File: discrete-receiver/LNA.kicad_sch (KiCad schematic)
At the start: 6 parts, among them U16 PSA4-5043_

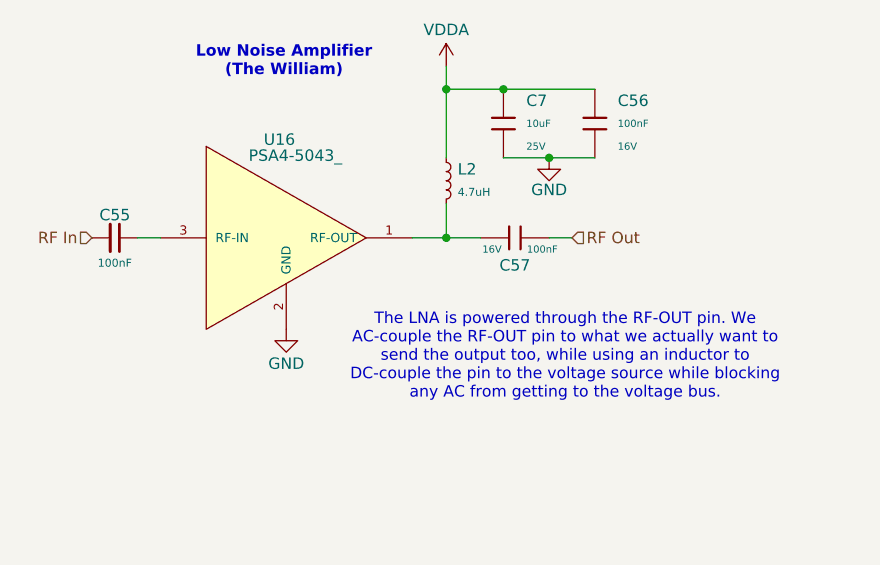
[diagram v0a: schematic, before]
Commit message: Parts on receiver page have been JLC'd and given footprints
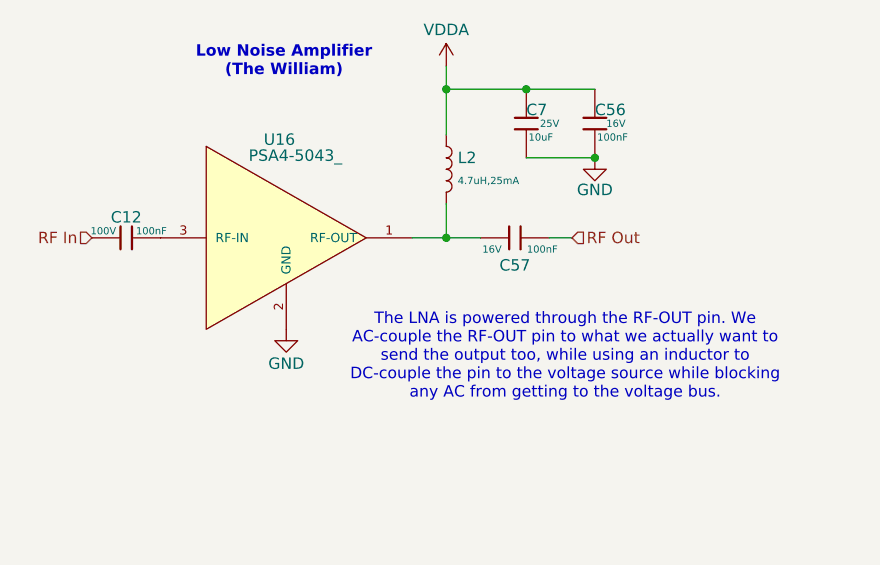
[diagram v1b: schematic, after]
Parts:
- removed C55: 100nF, symbol Device:C_Small
- removed L2: 4.7uH, symbol Device:L_Small
- added C12: 100nF, PCM_JLCPCB:C_0805, symbol PCM_JLCPCB-Capacitors:0805,100nF
- added L2: 4.7uH,25mA, PCM_JLCPCB:L_1206, symbol PCM_JLCPCB-Inductors:4.7uH,25mA
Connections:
- net RF In: now also C12.1
- net VDDA: now also L2.1
- net at C57.1, U16.1 (RF-OUT): now also L2.2
- net at U16.3 (RF-IN): now also C12.2
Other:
- moved on the sheet: C7

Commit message: Started to redo power
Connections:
- net VDDA renamed +5V_A
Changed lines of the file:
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@@
 			)
 		)
-		(property "Value" "VDDA"
+		(property "Value" "+5V_A"
 			(at 147.32 78.486 0)
 			(show_name no)

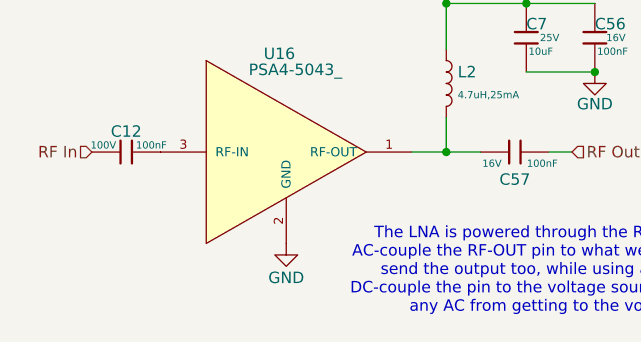
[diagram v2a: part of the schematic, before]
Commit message: Redone draft of power page
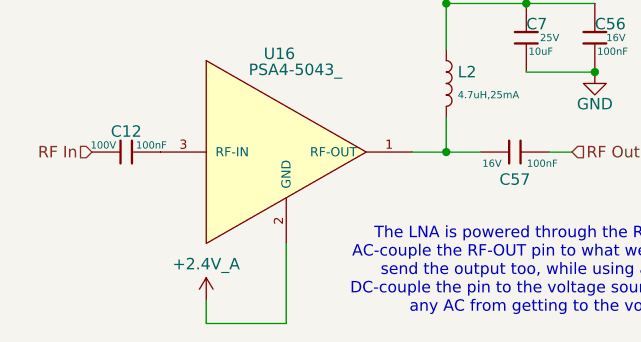
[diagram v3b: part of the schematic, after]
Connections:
- net GND: no longer U16.2 (GND), U16.4 (GND__1)
- new net +2.4V_A: U16.2 (GND), U16.4 (GND__1)
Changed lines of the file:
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@@
+	(wire
+		(pts
+			(xy 129.54 120.65) (xy 129.54 111.76)
+		)
+		(stroke
+			(width 0)
+			(type default)
+		)
+	)
 	(wire
 		(pts
@@
 		(pts
 			(xy 156.21 92.71) (xy 163.83 92.71)
+		)
+		(stroke
+			(width 0)
+			(type default)
+		)
+	)
+	(wire
+		(pts
+			(xy 120.65 120.65) (xy 129.54 120.65)
+		)
+		(stroke
+			(width 0)
+			(type default)
+		)
+	)
+	(wire
+		(pts
+			(xy 120.65 118.11) (xy 120.65 120.65)
 		)
 		(stroke
@@
 			)
 			(justify left)
+		)
+	)
+	(symbol
+		(lib_id "power:+5V")
+		(at 120.65 118.11 0)
+		(unit 1)
+		(body_style 1)
+		(exclude_from_sim no)
+		(in_bom yes)
+		(on_board yes)
+		(in_pos_files yes)
+		(dnp no)
+		(property "Reference" "#PWR0129"
+			(at 120.65 121.92 0)
+			(hide yes)
+			(show_name no)
+			(do_not_autoplace no)
+			(effects
+				(font
+					(size 1.27 1.27)
+				)
+			)
+		)
+		(property "Value" "+2.4V_A"
+			(at 120.65 114.046 0)
+			(show_name no)
+			(do_not_autoplace no)
+			(effects
+				(font
+					(size 1.27 1.27)
+				)
+			)
+		)
+		(property "Footprint" ""
+			(at 120.65 118.11 0)
+			(hide yes)
+			(show_name no)
+			(do_not_autoplace no)
+			(effects
+				(font
+					(size 1.27 1.27)
+				)
+			)
+		)
+		(property "Datasheet" ""
+			(at 120.65 118.11 0)
+			(hide yes)
+			(show_name no)
+			(do_not_autoplace no)
+			(effects
+				(font
+					(size 1.27 1.27)
+				)
+			)
+		)
+		(property "Description" "Power symbol creates a global label with name \"+5V\""
+			(at 120.65 118.11 0)
+			(hide yes)
+			(show_name no)
+			(do_not_autoplace no)
+			(effects
+				(font
+					(size 1.27 1.27)
+				)
+			)
+		)
+		(pin "1"
+		)
+		(instances
+			(project "diode_tayloe_sdr"
+				(path "/d18d178d-3f10-4d68-9036-eae71a7d091a/c96fbd90-62d0-401a-a1f5-d4c4d983c9a4/0811a985-c39e-470e-b379-1c06ccf39cf9"
+					(reference "#PWR0129")
+					(unit 1)
+				)
+			)
 		)
 	)
@@
 					(unit 1)
 				)
-			)
-		)
-	)
-	(symbol
-		(lib_id "power:GND")
-		(at 129.54 111.76 0)
-		(unit 1)
-		(body_style 1)
-		(exclude_from_sim no)
-		(in_bom yes)
-		(on_board yes)
-		(in_pos_files yes)
-		(dnp no)
-		(property "Reference" "#PWR047"
-			(at 129.54 118.11 0)
-			(hide yes)
-			(show_name no)
-			(do_not_autoplace no)
-			(effects
-				(font
-					(size 1.27 1.27)
-				)
-			)
-		)
-		(property "Value" "GND"
-			(at 129.54 115.57 0)
-			(show_name no)
-			(do_not_autoplace no)
-			(effects
-				(font
-					(size 1.27 1.27)
-				)
-			)
-		)
-		(property "Footprint" ""
-			(at 129.54 111.76 0)
-			(hide yes)
-			(show_name no)
-			(do_not_autoplace no)
-			(effects
-				(font
-					(size 1.27 1.27)
-				)
-			)
-		)
-		(property "Datasheet" ""
-			(at 129.54 111.76 0)
-			(hide yes)
-			(show_name no)
-			(do_not_autoplace no)
-			(effects
-				(font
-					(size 1.27 1.27)
-				)
-			)
-		)
-		(property "Description" "Power symbol creates a global label with name \"GND\" , ground"
-			(at 129.54 111.76 0)
-			(hide yes)
-			(show_name no)
-			(do_not_autoplace no)
-			(effects
-				(font
-					(size 1.27 1.27)
-				)
-			)
-		)
-		(pin "1"
-		)
-		(instances
-			(project "diode_tayloe_sdr"
-				(path "/d18d178d-3f10-4d68-9036-eae71a7d091a/c96fbd90-62d0-401a-a1f5-d4c4d983c9a4/0811a985-c39e-470e-b379-1c06ccf39cf9"
-					(reference "#PWR047")
-					(unit 1)
-				)

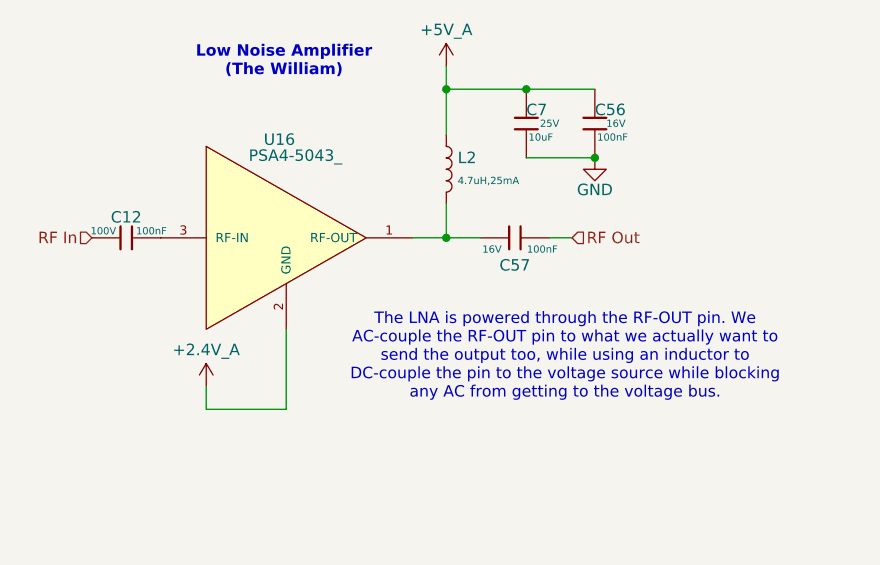
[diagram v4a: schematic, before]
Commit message: Added bypass capacitors to places on the 2.4V_A bus.
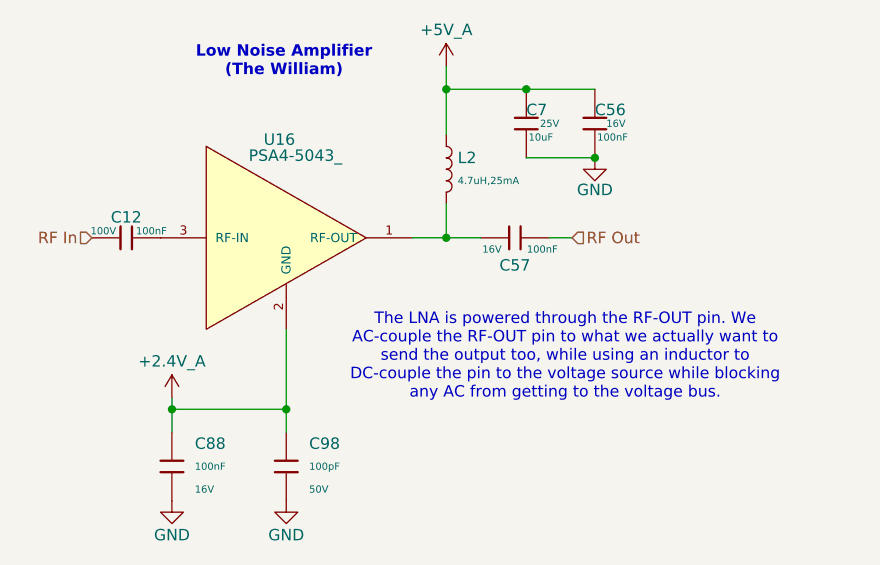
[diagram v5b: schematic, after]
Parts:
- added C88: 100nF, PCM_JLCPCB:C_0402, symbol PCM_JLCPCB-Capacitors:0402,100nF
- added C98: 100pF, PCM_JLCPCB:C_0603, symbol PCM_JLCPCB-Capacitors:0603,100pF
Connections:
- net +2.4V_A: now also C88.1, C98.1
- net GND: now also C88.2, C98.2

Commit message: all parts now have footprints
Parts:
- U16: footprint PSA4-5043_:PSA4-5043_ -> sdr_project:PSA4-5043_
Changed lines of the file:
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@@
 		)
 		(instances
-			(project "tayloe_detector"
+			(project "diode_tayloe_sdr"
 				(path "/d18d178d-3f10-4d68-9036-eae71a7d091a/c96fbd90-62d0-401a-a1f5-d4c4d983c9a4/0811a985-c39e-470e-b379-1c06ccf39cf9"
 					(reference "C98")
@@
 		)
 		(instances
-			(project "tayloe_detector"
+			(project "diode_tayloe_sdr"
 				(path "/d18d178d-3f10-4d68-9036-eae71a7d091a/c96fbd90-62d0-401a-a1f5-d4c4d983c9a4/0811a985-c39e-470e-b379-1c06ccf39cf9"
 					(reference "#PWR0129")
@@
 		)
 		(instances
-			(project "tayloe_detector"
+			(project "diode_tayloe_sdr"
 				(path "/d18d178d-3f10-4d68-9036-eae71a7d091a/c96fbd90-62d0-401a-a1f5-d4c4d983c9a4/0811a985-c39e-470e-b379-1c06ccf39cf9"
 					(reference "#PWR0117")
@@
 		)
 		(instances
-			(project "tayloe_detector"
+			(project "diode_tayloe_sdr"
 				(path "/d18d178d-3f10-4d68-9036-eae71a7d091a/c96fbd90-62d0-401a-a1f5-d4c4d983c9a4/0811a985-c39e-470e-b379-1c06ccf39cf9"
 					(reference "C88")
@@
 		)
 		(instances
-			(project "tayloe_detector"
+			(project "diode_tayloe_sdr"
 				(path "/d18d178d-3f10-4d68-9036-eae71a7d091a/c96fbd90-62d0-401a-a1f5-d4c4d983c9a4/0811a985-c39e-470e-b379-1c06ccf39cf9"
 					(reference "#PWR0123")
@@
 		)
 		(instances
-			(project "tayloe_detector"
+			(project "diode_tayloe_sdr"
 				(path "/d18d178d-3f10-4d68-9036-eae71a7d091a/c96fbd90-62d0-401a-a1f5-d4c4d983c9a4/0811a985-c39e-470e-b379-1c06ccf39cf9"
 					(reference "#PWR039")
@@
 			)
 		)
-		(property "Footprint" "PSA4-5043_:PSA4-5043_"
+		(property "Footprint" "sdr_project:PSA4-5043_"
 			(at 128.27 101.6 0)
 			(hide yes)
@@
 		)
 		(instances
-			(project "tayloe_detector"
+			(project "diode_tayloe_sdr"
 				(path "/d18d178d-3f10-4d68-9036-eae71a7d091a/c96fbd90-62d0-401a-a1f5-d4c4d983c9a4/0811a985-c39e-470e-b379-1c06ccf39cf9"
 					(reference "U16")
@@
 		)
 		(instances
-			(project "tayloe_detector"
+			(project "diode_tayloe_sdr"
 				(path "/d18d178d-3f10-4d68-9036-eae71a7d091a/c96fbd90-62d0-401a-a1f5-d4c4d983c9a4/0811a985-c39e-470e-b379-1c06ccf39cf9"
 					(reference "C57")
@@
 		)
 		(instances
-			(project "tayloe_detector"
+			(project "diode_tayloe_sdr"
 				(path "/d18d178d-3f10-4d68-9036-eae71a7d091a/c96fbd90-62d0-401a-a1f5-d4c4d983c9a4/0811a985-c39e-470e-b379-1c06ccf39cf9"
 					(reference "C7")
@@
 		)
 		(instances
-			(project "tayloe_detector"
+			(project "diode_tayloe_sdr"
 				(path "/d18d178d-3f10-4d68-9036-eae71a7d091a/c96fbd90-62d0-401a-a1f5-d4c4d983c9a4/0811a985-c39e-470e-b379-1c06ccf39cf9"
 					(reference "C12")
@@
 		)
 		(instances
-			(project "tayloe_detector"
+			(project "diode_tayloe_sdr"
 				(path "/d18d178d-3f10-4d68-9036-eae71a7d091a/c96fbd90-62d0-401a-a1f5-d4c4d983c9a4/0811a985-c39e-470e-b379-1c06ccf39cf9"
 					(reference "C56")
@@
 		)
 		(instances
-			(project "tayloe_detector"
+			(project "diode_tayloe_sdr"
 				(path "/d18d178d-3f10-4d68-9036-eae71a7d091a/c96fbd90-62d0-401a-a1f5-d4c4d983c9a4/0811a985-c39e-470e-b379-1c06ccf39cf9"
 					(reference "L2")
@@
 		)
 		(instances
-			(project "tayloe_detector"
+			(project "diode_tayloe_sdr"
 				(path "/d18d178d-3f10-4d68-9036-eae71a7d091a/c96fbd90-62d0-401a-a1f5-d4c4d983c9a4/0811a985-c39e-470e-b379-1c06ccf39cf9"
 					(reference "#PWR0114")
